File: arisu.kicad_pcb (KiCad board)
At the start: 2 copper layers, 162 parts, among them J1 USB_B_Micro, J10 PF6, J11 PF7, J2 MISO, J3 VCC, J4 SCK, J5 MOSI, J6 RES, J7 GND, J8 PF4, J9 PF5, SW1 SW_Push, SW10 SW_Push, SW11 SW_Push, SW12 SW_Push, SW13 SW_Push, SW14 SW_Push, SW15 SW_Push, SW16 SW_Push, SW17 SW_Push, SW18 SW_Push, SW19 SW_Push, SW2 SW_Push, SW20 SW_Push, SW21 SW_Push, SW22 SW_Push, SW23 SW_Push, SW24 SW_Push, SW25 SW_Push, SW26 SW_Push, SW27 SW_Push, SW28 SW_Push, SW29 SW_Push, SW3 SW_Push, SW30 SW_Push, SW31 SW_Push, SW32 SW_Push, SW33 SW_Push, SW34 SW_Push, SW35 SW_Push, SW36 SW_Push, SW37 SW_Push, SW38 SW_Push, SW39 SW_Push, SW4 SW_Push, SW40 SW_Push, SW41 SW_Push, SW42 SW_Push, SW43 SW_Push, SW44 SW_Push, SW45 SW_Push, SW46 SW_Push, SW47 SW_Push, SW48 SW_Push, SW49 SW_Push, SW5 SW_Push, SW50 SW_Push, SW51 SW_Push, SW52 SW_Push, SW53 SW_Push, SW54 SW_Push, SW55 SW_Push, SW56 SW_Push, SW57 SW_Push, SW58 SW_Push, SW59 SW_Push, SW6 SW_Push, SW60 SW_Push, SW61 SW_Push, SW62 SW_Push, SW63 SW_Push, SW64 SW_Push, SW65 SW_Push, SW66 SW_Push, SW67 SW_Push, SW7 SW_Push, SW8 SW_Push, SW9 SW_Push, U1 USBLC6-2SC6, U2 ATmega32U4-AU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

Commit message: Draw Edge.Cuts
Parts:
- moved J1 160.8 mm to (175.5, 26.4), turned to 180 degrees
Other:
- board outline added: 339.1 x 118.7 mm
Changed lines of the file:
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@@
   (general
     (thickness 1.6)
-    (drawings 1368)
+    (drawings 1380)
     (tracks 0)
     (zones 0)
@@
     (41 Cmts.User user)
     (42 Eco1.User user)
-    (43 Eco2.User user)
+    (43 Eco2.User user hide)
     (44 Edge.Cuts user)
     (45 Margin user)
@@
   )
   (module Connectors_USB:USB_Micro-B_Molex-105017-0001 (layer F.Cu)
-    (at 19.665001 -13.444999)
+    (at 175.509855 26.358 180)
     (descr http://www.molex.com/pdm_docs/sd/1050170001_sd.pdf)
     (tags "Micro-USB SMD Typ-B")
     (attr smd)
-    (fp_text reference J1 (at 0 -4) (layer F.SilkS)
+    (fp_text reference J1 (at 0 -4 180) (layer F.SilkS)
       (effects (font (size 1 1) (thickness 0.15)))
     )
-    (fp_text value USB_B_Micro (at 0.3 3.45) (layer F.Fab)
+    (fp_text value USB_B_Micro (at 0.3 3.45 180) (layer F.Fab)
       (effects (font (size 1 1) (thickness 0.15)))
     )
@@
     (fp_line (start -4.4 -3.35) (end 4.4 -3.35) (layer F.CrtYd) (width 0.05))
     (fp_line (start -4.4 2.75) (end -4.4 -3.35) (layer F.CrtYd) (width 0.05))
-    (fp_text user "PCB Edge" (at 0 1.8) (layer Dwgs.User)
+    (fp_text user "PCB Edge" (at 0 1.8 180) (layer Dwgs.User)
       (effects (font (size 0.5 0.5) (thickness 0.08)))
     )
@@
     (fp_line (start 3.9 -0.8) (end 3.9 -2.65) (layer F.SilkS) (width 0.12))
     (fp_line (start 3.9 -2.65) (end 3.45 -2.65) (layer F.SilkS) (width 0.12))
-    (fp_text user %R (at 0 0) (layer F.Fab)
+    (fp_text user %R (at 0 0 180) (layer F.Fab)
       (effects (font (size 1 1) (thickness 0.15)))
     )
@@
     (fp_line (start -1.5 -3.01) (end -1.5 -2.8) (layer F.Fab) (width 0.1))
     (fp_line (start -1.1 -3.01) (end -1.1 -2.8) (layer F.Fab) (width 0.1))
-    (pad 6 smd rect (at 1 0.35) (size 1.5 1.9) (layers F.Cu F.Paste F.Mask)
+    (pad 6 smd rect (at 1 0.35 180) (size 1.5 1.9) (layers F.Cu F.Paste F.Mask)
       (net 1 GND))
-    (pad 6 thru_hole circle (at -2.5 -2.35) (size 1.45 1.45) (drill 0.85) (layers *.Cu *.Mask)
+    (pad 6 thru_hole circle (at -2.5 -2.35 180) (size 1.45 1.45) (drill 0.85) (layers *.Cu *.Mask)
       (net 1 GND))
-    (pad 2 smd rect (at -0.65 -2.35) (size 0.4 1.35) (layers F.Cu F.Paste F.Mask)
+    (pad 2 smd rect (at -0.65 -2.35 180) (size 0.4 1.35) (layers F.Cu F.Paste F.Mask)
       (net 80 "Net-(J1-Pad2)"))
-    (pad 1 smd rect (at -1.3 -2.35) (size 0.4 1.35) (layers F.Cu F.Paste F.Mask)
+    (pad 1 smd rect (at -1.3 -2.35 180) (size 0.4 1.35) (layers F.Cu F.Paste F.Mask)
       (net 4 VCC))
-    (pad 5 smd rect (at 1.3 -2.35) (size 0.4 1.35) (layers F.Cu F.Paste F.Mask)
+    (pad 5 smd rect (at 1.3 -2.35 180) (size 0.4 1.35) (layers F.Cu F.Paste F.Mask)
       (net 1 GND))
-    (pad 4 smd rect (at 0.65 -2.35) (size 0.4 1.35) (layers F.Cu F.Paste F.Mask)
+    (pad 4 smd rect (at 0.65 -2.35 180) (size 0.4 1.35) (layers F.Cu F.Paste F.Mask)
       (net 79 "Net-(J1-Pad4)"))
-    (pad 3 smd rect (at 0 -2.35) (size 0.4 1.35) (layers F.Cu F.Paste F.Mask)
+    (pad 3 smd rect (at 0 -2.35 180) (size 0.4 1.35) (layers F.Cu F.Paste F.Mask)
       (net 78 "Net-(J1-Pad3)"))
-    (pad 6 thru_hole circle (at 2.5 -2.35) (size 1.45 1.45) (drill 0.85) (layers *.Cu *.Mask)
+    (pad 6 thru_hole circle (at 2.5 -2.35 180) (size 1.45 1.45) (drill 0.85) (layers *.Cu *.Mask)
       (net 1 GND))
-    (pad 6 smd rect (at -1 0.35) (size 1.5 1.9) (layers F.Cu F.Paste F.Mask)
+    (pad 6 smd rect (at -1 0.35 180) (size 1.5 1.9) (layers F.Cu F.Paste F.Mask)
       (net 1 GND))
-    (pad 6 thru_hole oval (at -3.5 0.35 180) (size 1.2 1.9) (drill oval 0.6 1.3) (layers *.Cu *.Mask)
+    (pad 6 thru_hole oval (at -3.5 0.35) (size 1.2 1.9) (drill oval 0.6 1.3) (layers *.Cu *.Mask)
       (net 1 GND))
-    (pad 6 thru_hole oval (at 3.5 0.35) (size 1.2 1.9) (drill oval 0.6 1.3) (layers *.Cu *.Mask)
+    (pad 6 thru_hole oval (at 3.5 0.35 180) (size 1.2 1.9) (drill oval 0.6 1.3) (layers *.Cu *.Mask)
       (net 1 GND))
-    (pad 6 smd rect (at 2.9 0.35) (size 1.2 1.9) (layers F.Cu F.Mask)
+    (pad 6 smd rect (at 2.9 0.35 180) (size 1.2 1.9) (layers F.Cu F.Mask)
       (net 1 GND))
-    (pad 6 smd rect (at -2.9 0.35) (size 1.2 1.9) (layers F.Cu F.Mask)
+    (pad 6 smd rect (at -2.9 0.35 180) (size 1.2 1.9) (layers F.Cu F.Mask)
       (net 1 GND))
     (model ${KISYS3DMOD}/Connectors_USB.3dshapes/USB_Micro-B_Molex-105017-0001.wrl
@@
     )
   )
+  (gr_arc (start 362.499949 127.207503) (end 364.499949 127.207503) (angle 90) (layer Edge.Cuts) (width 0.15))
+  (gr_arc (start 362.499949 26.432509) (end 364.499949 26.432509) (angle -90) (layer Edge.Cuts) (width 0.15))
+  (gr_arc (start 27.4125 26.432509) (end 25.4125 26.432509) (angle 90) (layer Edge.Cuts) (width 0.15))
+  (gr_arc (start 27.4125 127.207503) (end 25.4125 127.207503) (angle -90) (layer Edge.Cuts) (width 0.15))
+  (gr_line (start 182.63 143.125232) (end 248.11 129.207503) (layer Edge.Cuts) (width 0.15))
+  (gr_line (start 168.6 143.125232) (end 182.63 143.125232) (layer Edge.Cuts) (width 0.15))
+  (gr_line (start 103.1267 129.207503) (end 168.6 143.125232) (layer Edge.Cuts) (width 0.15))
+  (gr_line (start 248.11 129.207503) (end 362.499949 129.207503) (layer Edge.Cuts) (width 0.15))
+  (gr_line (start 27.4125 129.207503) (end 103.1267 129.207503) (layer Edge.Cuts) (width 0.15))
+  (gr_line (start 27.4125 24.432509) (end 362.499949 24.432509) (layer Edge.Cuts) (width 0.15))
+  (gr_line (start 364.499949 26.432509) (end 364.499949 127.207503) (layer Edge.Cuts) (width 0.15))
+  (gr_line (start 25.4125 26.432509) (end 25.4125 127.207503) (layer Edge.Cuts) (width 0.15))
   (gr_line (start 84.24337 63.547863) (end 84.012299 63.192045) (layer Eco2.User) (width 0.2))
   (gr_line (start 124.065742 58.006322) (end 124.42156 57.775252) (layer Eco2.User) (width 0.2))

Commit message: Arrange core components
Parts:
- C1, C2, C3, C4, C5, C6, C7, C8, C9, J1, J10, J11, J2, J3, J4, J5, J6, J7, J8, J9, R1, R2, R3, R4, SWR1, U1, U2, Y1: moved to B.Cu
- moved J3 191.0 mm to (218.2, 26.4)
- moved J2 189.6 mm to (220.7, 26.4)
- moved SWR1 185.3 mm to (201.2, 29.0), turned to 180 degrees
- moved J5 185.2 mm to (213.1, 26.4)
- moved J7 183.8 mm to (208.0, 26.4)
- moved J4 179.6 mm to (215.6, 26.4)
- moved R3 179.4 mm to (194.3, 29.0), turned to 270 degrees
- moved J6 176.1 mm to (210.6, 26.4)
- moved Y1 176.0 mm to (194.8, 38.4), turned to 180 degrees
- moved C1 171.8 mm to (199.8, 38.4), turned to 270 degrees
- moved C9 168.6 mm to (185.7, 37.8), turned to 90 degrees
- moved C2 168.5 mm to (189.8, 38.4), turned to 270 degrees
- moved C7 165.4 mm to (180.8, 50.3)
- moved C3 164.0 mm to (183.1, 30.2), turned to 90 degrees
- moved C4 159.2 mm to (181.1, 30.2), turned to 90 degrees
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
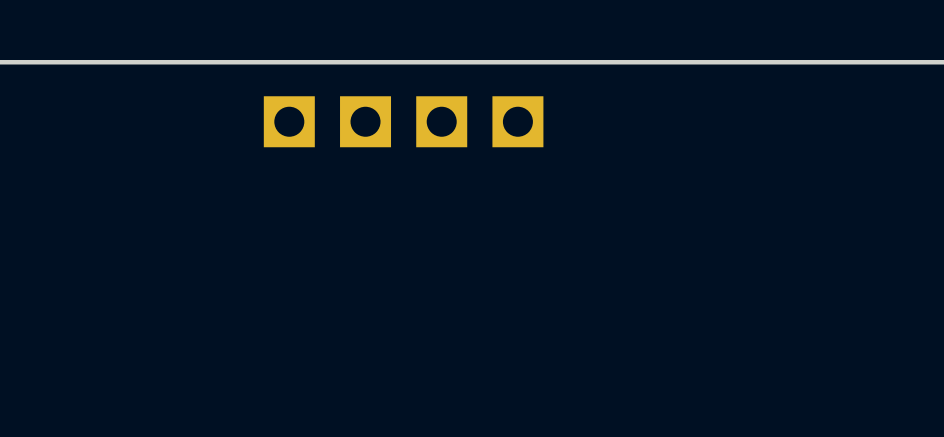
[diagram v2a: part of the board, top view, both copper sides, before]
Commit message: Add D+/D- pin header to Pcbnew
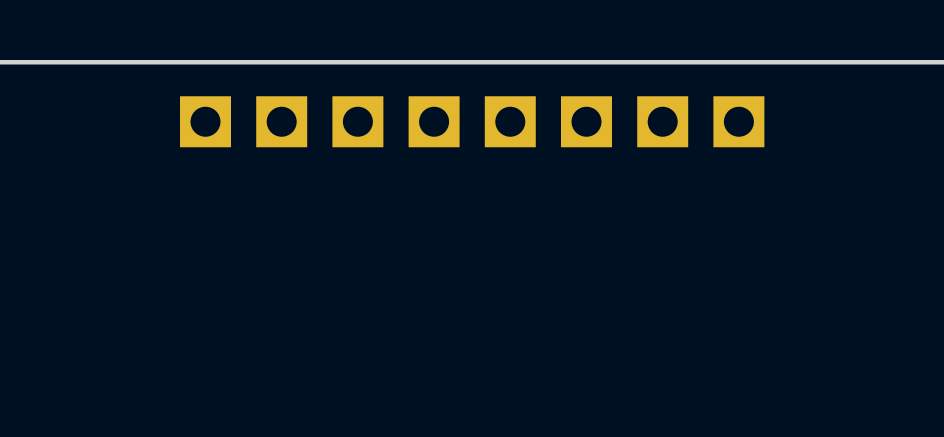
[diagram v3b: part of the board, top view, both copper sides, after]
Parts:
- added J12: VCC, Pin_Headers:Pin_Header_Straight_1x01_Pitch2.54mm, B.Cu at (151.4, 26.4)
- added J13: D+, Pin_Headers:Pin_Header_Straight_1x01_Pitch2.54mm, B.Cu at (146.3, 26.4)
- added J14: D-, Pin_Headers:Pin_Header_Straight_1x01_Pitch2.54mm, B.Cu at (148.8, 26.4)
- added J15: GND, Pin_Headers:Pin_Header_Straight_1x01_Pitch2.54mm, B.Cu at (143.8, 26.4)
- moved J8 2.79 mm to (141.2, 26.4)
- moved J9 2.79 mm to (138.7, 26.4)
- moved J10 2.79 mm to (136.1, 26.4)
- moved J11 2.79 mm to (133.6, 26.4)
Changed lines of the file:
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@@
     (tracks 0)
     (zones 0)
-    (modules 162)
+    (modules 166)
     (nets 108)
   )
@@
   )
   (module Pin_Headers:Pin_Header_Straight_1x01_Pitch2.54mm (layer B.Cu)
-    (at 144.018 26.416)
+    (at 141.224 26.416)
     (descr "Through hole straight pin header, 1x01, 2.54mm pitch, single row")
     (tags "Through hole pin header THT 1x01 2.54mm single row")
@@
   )
   (module Pin_Headers:Pin_Header_Straight_1x01_Pitch2.54mm (layer B.Cu)
-    (at 141.478 26.416)
+    (at 138.684 26.416)
     (descr "Through hole straight pin header, 1x01, 2.54mm pitch, single row")
     (tags "Through hole pin header THT 1x01 2.54mm single row")
@@
   )
   (module Pin_Headers:Pin_Header_Straight_1x01_Pitch2.54mm (layer B.Cu)
-    (at 138.938 26.416)
+    (at 136.144 26.416)
     (descr "Through hole straight pin header, 1x01, 2.54mm pitch, single row")
     (tags "Through hole pin header THT 1x01 2.54mm single row")
@@
   )
   (module Pin_Headers:Pin_Header_Straight_1x01_Pitch2.54mm (layer B.Cu)
-    (at 136.398 26.416)
+    (at 133.604 26.416)
     (descr "Through hole straight pin header, 1x01, 2.54mm pitch, single row")
     (tags "Through hole pin header THT 1x01 2.54mm single row")
@@
       (at (xyz 0 0 0))
       (scale (xyz 1 1 1))
+      (rotate (xyz 0 0 0))
+    )
+  )
+  (module Pin_Headers:Pin_Header_Straight_1x01_Pitch2.54mm (layer B.Cu)
+    (at 151.384 26.416)
+    (descr "Through hole straight pin header, 1x01, 2.54mm pitch, single row")
+    (tags "Through hole pin header THT 1x01 2.54mm single row")
+    (fp_text reference J12 (at 0 2.33) (layer B.SilkS)
+      (effects (font (size 1 1) (thickness 0.15)) (justify mirror))
+    )
+    (fp_text value VCC (at 0 -2.33) (layer B.Fab)
+      (effects (font (size 1 1) (thickness 0.15)) (justify mirror))
+    )
+    (fp_line (start -0.635 1.27) (end 1.27 1.27) (layer B.Fab) (width 0.1))
+    (fp_line (start 1.27 1.27) (end 1.27 -1.27) (layer B.Fab) (width 0.1))
+    (fp_line (start 1.27 -1.27) (end -1.27 -1.27) (layer B.Fab) (width 0.1))
+    (fp_line (start -1.27 -1.27) (end -1.27 0.635) (layer B.Fab) (width 0.1))
+    (fp_line (start -1.27 0.635) (end -0.635 1.27) (layer B.Fab) (width 0.1))
+    (fp_line (start -1.33 -1.33) (end 1.33 -1.33) (layer B.SilkS) (width 0.12))
+    (fp_line (start -1.33 -1.27) (end -1.33 -1.33) (layer B.SilkS) (width 0.12))
+    (fp_line (start 1.33 -1.27) (end 1.33 -1.33) (layer B.SilkS) (width 0.12))
+    (fp_line (start -1.33 -1.27) (end 1.33 -1.27) (layer B.SilkS) (width 0.12))
+    (fp_line (start -1.33 0) (end -1.33 1.33) (layer B.SilkS) (width 0.12))
+    (fp_line (start -1.33 1.33) (end 0 1.33) (layer B.SilkS) (width 0.12))
+    (fp_line (start -1.8 1.8) (end -1.8 -1.8) (layer B.CrtYd) (width 0.05))
+    (fp_line (start -1.8 -1.8) (end 1.8 -1.8) (layer B.CrtYd) (width 0.05))
+    (fp_line (start 1.8 -1.8) (end 1.8 1.8) (layer B.CrtYd) (width 0.05))
+    (fp_line (start 1.8 1.8) (end -1.8 1.8) (layer B.CrtYd) (width 0.05))
+    (fp_text user %R (at 0 0 -90) (layer B.Fab)
+      (effects (font (size 1 1) (thickness 0.15)) (justify mirror))
+    )
+    (pad 1 thru_hole rect (at 0 0) (size 1.7 1.7) (drill 1) (layers *.Cu *.Mask)
+      (net 4 VCC))
+    (model ${KISYS3DMOD}/Pin_Headers.3dshapes/Pin_Header_Straight_1x01_Pitch2.54mm.wrl
+      (at (xyz 0 0 0))
+      (scale (xyz 1 1 1))
+      (rotate (xyz 0 0 0))
+    )
+  )
+  (module Pin_Headers:Pin_Header_Straight_1x01_Pitch2.54mm (layer B.Cu)
+    (at 146.304 26.416)
+    (descr "Through hole straight pin header, 1x01, 2.54mm pitch, single row")
+    (tags "Through hole pin header THT 1x01 2.54mm single row")
+    (fp_text reference J13 (at 0 2.33) (layer B.SilkS)
+      (effects (font (size 1 1) (thickness 0.15)) (justify mirror))
+    )
+    (fp_text value D+ (at 0 -2.33) (layer B.Fab)
+      (effects (font (size 1 1) (thickness 0.15)) (justify mirror))
+    )
+    (fp_line (start -0.635 1.27) (end 1.27 1.27) (layer B.Fab) (width 0.1))
+    (fp_line (start 1.27 1.27) (end 1.27 -1.27) (layer B.Fab) (width 0.1))
+    (fp_line (start 1.27 -1.27) (end -1.27 -1.27) (layer B.Fab) (width 0.1))
+    (fp_line (start -1.27 -1.27) (end -1.27 0.635) (layer B.Fab) (width 0.1))
+    (fp_line (start -1.27 0.635) (end -0.635 1.27) (layer B.Fab) (width 0.1))
+    (fp_line (start -1.33 -1.33) (end 1.33 -1.33) (layer B.SilkS) (width 0.12))
+    (fp_line (start -1.33 -1.27) (end -1.33 -1.33) (layer B.SilkS) (width 0.12))
+    (fp_line (start 1.33 -1.27) (end 1.33 -1.33) (layer B.SilkS) (width 0.12))
+    (fp_line (start -1.33 -1.27) (end 1.33 -1.27) (layer B.SilkS) (width 0.12))
+    (fp_line (start -1.33 0) (end -1.33 1.33) (layer B.SilkS) (width 0.12))
+    (fp_line (start -1.33 1.33) (end 0 1.33) (layer B.SilkS) (width 0.12))
+    (fp_line (start -1.8 1.8) (end -1.8 -1.8) (layer B.CrtYd) (width 0.05))
+    (fp_line (start -1.8 -1.8) (end 1.8 -1.8) (layer B.CrtYd) (width 0.05))
+    (fp_line (start 1.8 -1.8) (end 1.8 1.8) (layer B.CrtYd) (width 0.05))
+    (fp_line (start 1.8 1.8) (end -1.8 1.8) (layer B.CrtYd) (width 0.05))
+    (fp_text user %R (at 0 0 -90) (layer B.Fab)
+      (effects (font (size 1 1) (thickness 0.15)) (justify mirror))
+    )
+    (pad 1 thru_hole rect (at 0 0) (size 1.7 1.7) (drill 1) (layers *.Cu *.Mask)
+      (net 78 "Net-(J1-Pad3)"))
+    (model ${KISYS3DMOD}/Pin_Headers.3dshapes/Pin_Header_Straight_1x01_Pitch2.54mm.wrl
+      (at (xyz 0 0 0))
+      (scale (xyz 1 1 1))
+      (rotate (xyz 0 0 0))
+    )
+  )
+  (module Pin_Headers:Pin_Header_Straight_1x01_Pitch2.54mm (layer B.Cu)
+    (at 148.844 26.416)
+    (descr "Through hole straight pin header, 1x01, 2.54mm pitch, single row")
+    (tags "Through hole pin header THT 1x01 2.54mm single row")
+    (fp_text reference J14 (at 0 2.33) (layer B.SilkS)
+      (effects (font (size 1 1) (thickness 0.15)) (justify mirror))
+    )
+    (fp_text value D- (at 0 -2.33) (layer B.Fab)
+      (effects (font (size 1 1) (thickness 0.15)) (justify mirror))
+    )
+    (fp_text user %R (at 0 0 -90) (layer B.Fab)
+      (effects (font (size 1 1) (thickness 0.15)) (justify mirror))
+    )
+    (fp_line (start 1.8 1.8) (end -1.8 1.8) (layer B.CrtYd) (width 0.05))
+    (fp_line (start 1.8 -1.8) (end 1.8 1.8) (layer B.CrtYd) (width 0.05))
+    (fp_line (start -1.8 -1.8) (end 1.8 -1.8) (layer B.CrtYd) (width 0.05))
+    (fp_line (start -1.8 1.8) (end -1.8 -1.8) (layer B.CrtYd) (width 0.05))
+    (fp_line (start -1.33 1.33) (end 0 1.33) (layer B.SilkS) (width 0.12))
+    (fp_line (start -1.33 0) (end -1.33 1.33) (layer B.SilkS) (width 0.12))
+    (fp_line (start -1.33 -1.27) (end 1.33 -1.27) (layer B.SilkS) (width 0.12))
+    (fp_line (start 1.33 -1.27) (end 1.33 -1.33) (layer B.SilkS) (width 0.12))
+    (fp_line (start -1.33 -1.27) (end -1.33 -1.33) (layer B.SilkS) (width 0.12))
+    (fp_line (start -1.33 -1.33) (end 1.33 -1.33) (layer B.SilkS) (width 0.12))
+    (fp_line (start -1.27 0.635) (end -0.635 1.27) (layer B.Fab) (width 0.1))
+    (fp_line (start -1.27 -1.27) (end -1.27 0.635) (layer B.Fab) (width 0.1))
+    (fp_line (start 1.27 -1.27) (end -1.27 -1.27) (layer B.Fab) (width 0.1))
+    (fp_line (start 1.27 1.27) (end 1.27 -1.27) (layer B.Fab) (width 0.1))
+    (fp_line (start -0.635 1.27) (end 1.27 1.27) (layer B.Fab) (width 0.1))
+    (pad 1 thru_hole rect (at 0 0) (size 1.7 1.7) (drill 1) (layers *.Cu *.Mask)
+      (net 80 "Net-(J1-Pad2)"))
+    (model ${KISYS3DMOD}/Pin_Headers.3dshapes/Pin_Header_Straight_1x01_Pitch2.54mm.wrl
+      (at (xyz 0 0 0))
+      (scale (xyz 1 1 1))
+      (rotate (xyz 0 0 0))
+    )
+  )
+  (module Pin_Headers:Pin_Header_Straight_1x01_Pitch2.54mm (layer B.Cu)
+    (at 143.764 26.416)
+    (descr "Through hole straight pin header, 1x01, 2.54mm pitch, single row")
+    (tags "Through hole pin header THT 1x01 2.54mm single row")
+    (fp_text reference J15 (at 0 2.33) (layer B.SilkS)
+      (effects (font (size 1 1) (thickness 0.15)) (justify mirror))
+    )
+    (fp_text value GND (at 0 -2.33) (layer B.Fab)
+      (effects (font (size 1 1) (thickness 0.15)) (justify mirror))
+    )
+    (fp_text user %R (at 0 0 -90) (layer B.Fab)
+      (effects (font (size 1 1) (thickness 0.15)) (justify mirror))
+    )
+    (fp_line (start 1.8 1.8) (end -1.8 1.8) (layer B.CrtYd) (width 0.05))
+    (fp_line (start 1.8 -1.8) (end 1.8 1.8) (layer B.CrtYd) (width 0.05))
+    (fp_line (start -1.8 -1.8) (end 1.8 -1.8) (layer B.CrtYd) (width 0.05))
+    (fp_line (start -1.8 1.8) (end -1.8 -1.8) (layer B.CrtYd) (width 0.05))
+    (fp_line (start -1.33 1.33) (end 0 1.33) (layer B.SilkS) (width 0.12))
+    (fp_line (start -1.33 0) (end -1.33 1.33) (layer B.SilkS) (width 0.12))
+    (fp_line (start -1.33 -1.27) (end 1.33 -1.27) (layer B.SilkS) (width 0.12))
+    (fp_line (start 1.33 -1.27) (end 1.33 -1.33) (layer B.SilkS) (width 0.12))
+    (fp_line (start -1.33 -1.27) (end -1.33 -1.33) (layer B.SilkS) (width 0.12))
+    (fp_line (start -1.33 -1.33) (end 1.33 -1.33) (layer B.SilkS) (width 0.12))
+    (fp_line (start -1.27 0.635) (end -0.635 1.27) (layer B.Fab) (width 0.1))
+    (fp_line (start -1.27 -1.27) (end -1.27 0.635) (layer B.Fab) (width 0.1))
+    (fp_line (start 1.27 -1.27) (end -1.27 -1.27) (layer B.Fab) (width 0.1))
+    (fp_line (start 1.27 1.27) (end 1.27 -1.27) (layer B.Fab) (width 0.1))
+    (fp_line (start -0.635 1.27) (end 1.27 1.27) (layer B.Fab) (width 0.1))
+    (pad 1 thru_hole rect (at 0 0) (size 1.7 1.7) (drill 1) (layers *.Cu *.Mask)
+      (net 1 GND))
+    (model ${KISYS3DMOD}/Pin_Headers.3dshapes/Pin_Header_Straight_1x01_Pitch2.54mm.wrl
+      (at (xyz 0 0 0))
+      (scale (xyz 1 1 1))

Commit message: Define Design Rules
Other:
- net class Power added: clearance 0.2, trace_width 0.375, via_dia 0.8, via_drill 0.4
- rule via_min_drill: 0.3 -> 0.4
- rule via_min_size: 0.4 -> 0.7
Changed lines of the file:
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@@
   (setup
     (last_trace_width 0.25)
+    (user_trace_width 0.25)
+    (user_trace_width 0.375)
     (trace_clearance 0.2)
     (zone_clearance 0.508)
@@
     (via_size 0.8)
     (via_drill 0.4)
-    (via_min_size 0.4)
-    (via_min_drill 0.3)
+    (via_min_size 0.7)
+    (via_min_drill 0.4)
+    (user_via 0.8 0.4)
     (uvia_size 0.3)
     (uvia_drill 0.1)
@@
     (add_net D+)
     (add_net D-)
-    (add_net GND)
     (add_net "Net-(C4-Pad1)")
     (add_net "Net-(D1-Pad2)")
@@
     (add_net "Net-(U1-Pad3)")
     (add_net "Net-(U2-Pad42)")
-    (add_net VCC)
     (add_net XTAL1)
     (add_net XTAL2)
   )
+  (net_class Power ""
+    (clearance 0.2)
+    (trace_width 0.375)
+    (via_dia 0.8)
+    (via_drill 0.4)
+    (uvia_dia 0.3)
+    (uvia_drill 0.1)
+    (add_net GND)
+    (add_net VCC)
+  )
   (module Capacitors_SMD:C_0805_HandSoldering (layer B.Cu)
